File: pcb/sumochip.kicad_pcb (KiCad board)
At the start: 2 copper layers, 68.6 x 68.6 mm, 61 parts, among them P6 P5, Q5 OPTO_NPN

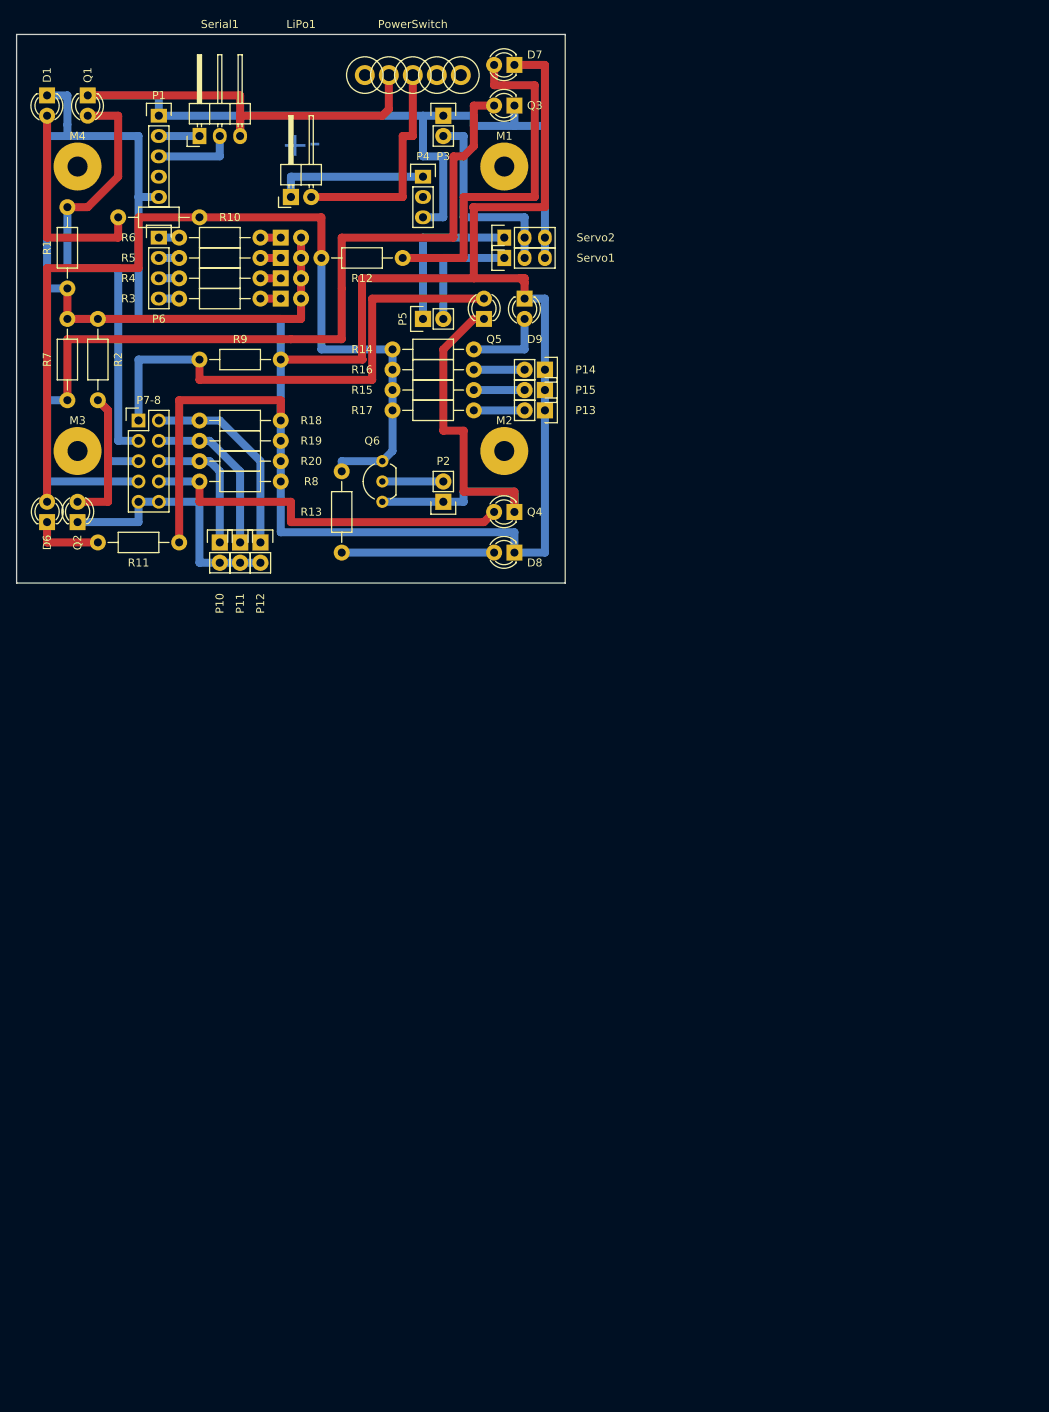
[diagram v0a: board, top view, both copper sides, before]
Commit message: Add SumoCHIP PCB v1.1 schematic and layout
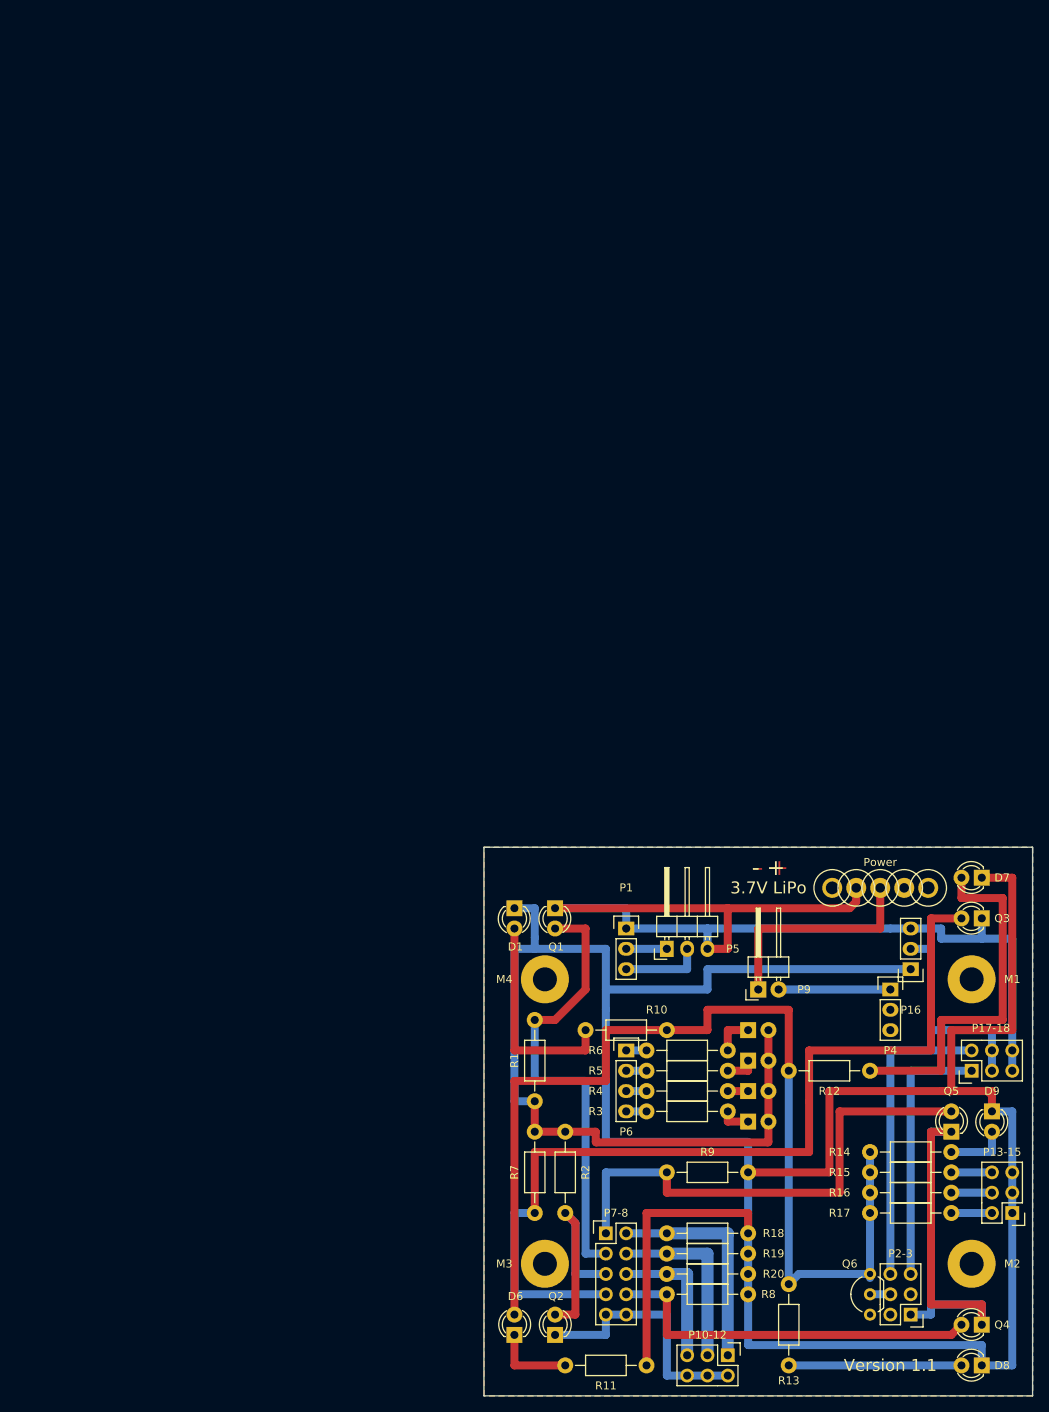
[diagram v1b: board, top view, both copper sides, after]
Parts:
- removed LiPo1: 3.7V, Pin_Headers:Pin_Header_Angled_1x02
- removed P10, P11, P12, P13, P14, P15, P2, P3: , Pin_Headers:Pin_Header_Straight_1x02
- removed Serial1: , Pin_Headers:Pin_Header_Angled_1x03
- removed Servo1, Servo2: , Pin_Headers:Pin_Header_Straight_1x03
- added P10-12: LineFollowPhoto, Pin_Headers:Pin_Header_Straight_2x03, F.Cu at (101.6, 177.8)
- added P13-15: LineFollowLED, Pin_Headers:Pin_Header_Straight_2x03, F.Cu at (137.2, 160.0)
- added P16: PowerHeader, Pin_Headers:Pin_Header_Straight_1x03, F.Cu at (124.5, 129.5)
- added P17-18: ServoPins, Pin_Headers:Pin_Header_Straight_2x03, F.Cu at (132.1, 142.2)
- added P2-3: ActuatorsHeader, Pin_Headers:Pin_Header_Straight_2x03, F.Cu at (124.5, 172.7)
- added P9: BatteryPins, Pin_Headers:Pin_Header_Angled_1x02, F.Cu at (105.4, 132.1)
- D1: value (none) -> EnemyFrontLeftLED
- D2, D3, D4, D5: value (none) -> LED
- D6: value (none) -> EnemyFrontRightLED
- D7: value (none) -> EnemyLeftLED
- D8: value (none) -> EnemyRightLED
- D9: value IR LED -> EnemyBackLED
- P1: value (none) -> SerialHeader; footprint Pin_Headers:Pin_Header_Straight_1x05 -> Pin_Headers:Pin_Header_Straight_1x03
- P4: value (none) -> BatteryHeader
- P5: value (none) -> SerialPins; footprint Pin_Headers:Pin_Header_Straight_1x02 -> Pin_Headers:Pin_Header_Angled_1x03
- P6: value P5 -> DiagnosticHeader
- P7-8: value (none) -> SensorsHeader
- Q1: value (none) -> EnemyFrontLeftPhoto
- Q2: value (none) -> EnemyFrontRightPhoto
- Q3: value (none) -> EnemyLeftPhoto
- Q4: value (none) -> EnemyRightPhoto
- Q5: value OPTO_NPN -> EnemyBackPhoto
- Q6: value (none) -> 2N7000
- R18, R19, R20: value 100k -> 10k
- moved R16 118.9 mm to (119.4, 157.5)
- moved Q6 118.5 mm to (119.4, 172.7)
- moved D2 118.3 mm to (104.1, 148.6)
- moved R11 118.3 mm to (91.4, 179.1)
- moved Q2 117.8 mm to (80.0, 175.3)
- moved Q5 117.2 mm to (129.5, 149.9)
- moved R2 117.2 mm to (81.3, 149.9)
- moved R7 117.2 mm to (77.5, 149.9)
- moved M1 117.2 mm to (132.1, 130.8)
- moved M2 117.2 mm to (132.1, 166.4)
- moved M3 117.2 mm to (78.7, 166.4)
- moved P4 117.2 mm to (121.9, 132.1)
- moved Q4 117.2 mm to (133.3, 174.0)
- moved R1 117.2 mm to (77.5, 146.1)
- moved R12 117.2 mm to (119.4, 142.2)
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- renumbered PowerSwitch to Power
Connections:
- P5 pad 1: Net-(P5-Pad1) -> Net-(P1-Pad2)
- P5 pad 2: Net-(P5-Pad2) -> Net-(P1-Pad3)
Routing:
- net +3.3V: track 340.6 -> 383.6 mm
- net Net-(P17-18-Pad2): track 0.00 -> 38.1 mm
- net Net-(P17-18-Pad1): track 0.00 -> 33.0 mm
- net Net-(P5-Pad1): track 20.3 -> 0.00 mm
- net Net-(D6-Pad2): track 116.1 -> 133.1 mm
- net Net-(P5-Pad2): track 15.2 -> 0.00 mm
- net GND: track 240.0 -> 231.5 mm
- net Net-(P4-Pad1): track 19.1 -> 14.0 mm
- net Net-(P2-3-Pad4): track 7.62 -> 2.54 mm
- net Net-(P10-12-Pad1): track 25.4 -> 28.4 mm
- net Net-(D9-Pad2): track 10.2 -> 7.62 mm
- net Net-(D8-Pad2): track 19.0 -> 21.6 mm
- net Net-(D5-Pad1): track 2.54 -> 5.08 mm
- net Net-(P10-12-Pad3): track 20.9 -> 23.1 mm
- net Net-(P7-8-Pad5): track 29.0 -> 27.7 mm
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- added copper zone on B.Cu, net GND
- added copper zone on F.Cu, net GND
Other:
- net class Locked removed
- net class Thick added: clearance 0.2, trace_width 1.5, via_dia 0.6, via_drill 0.4
- board text added: "- +"
- board text added: "3.7V LiPo"
- board text added: "SumoCHIP"
- board text added: "Version 1.1"
- board text added: "robot.itcollege.ee"
- board text removed: "+-"
